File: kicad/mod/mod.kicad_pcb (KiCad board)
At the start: 2 copper layers, 9 parts, among them J1 In, J2 Out, J3 Program Pins, U1 AP7384-33SA, U2 ATtiny402-SS

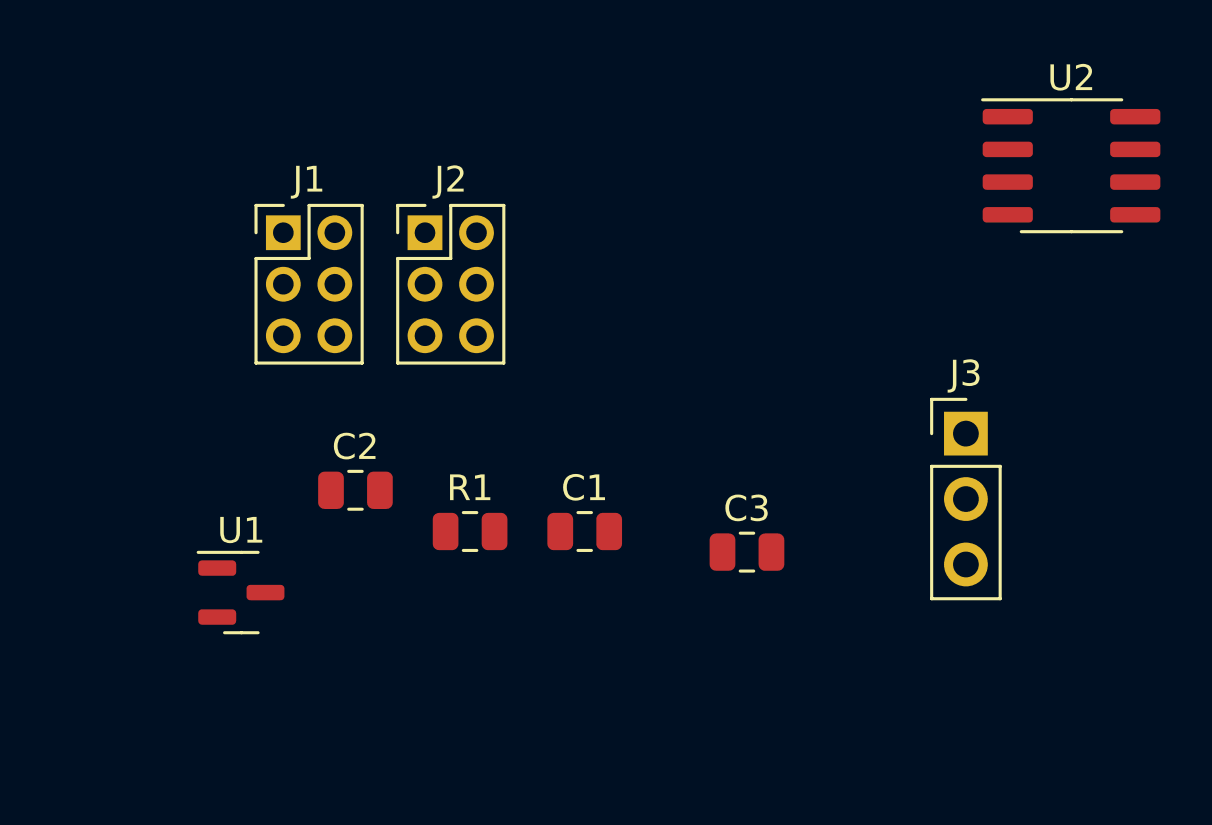
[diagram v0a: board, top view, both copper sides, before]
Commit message: Started layout
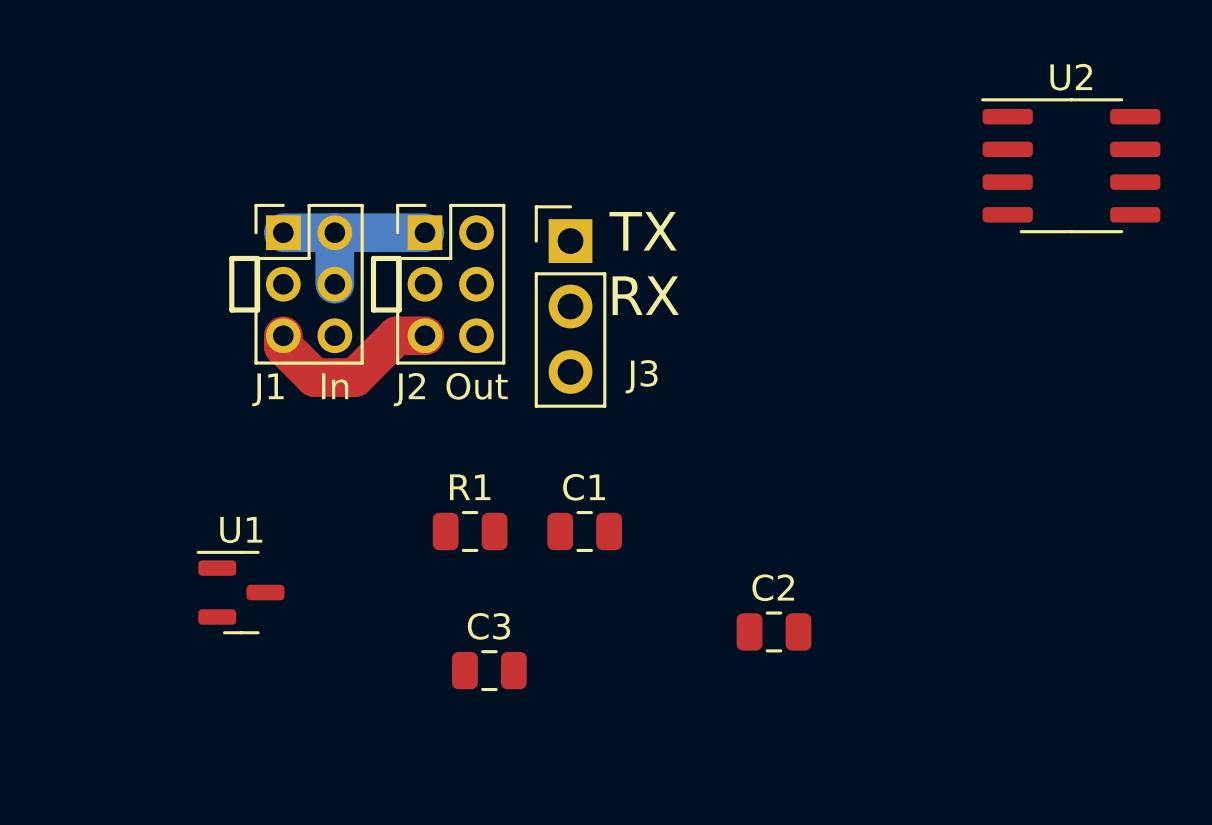
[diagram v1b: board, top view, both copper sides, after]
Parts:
- moved C2 17.2 mm to (147.1, 105.5)
- moved J3 17.1 mm to (139.2, 90.3)
- moved C3 11.0 mm to (136.0, 107.0)
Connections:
- J1 pad 1: +12V -> GND
- J1 pad 2: unconnected-(J1-Pad2) -> GND
- J1 pad 5: GND -> +12V
- J1 pad 6: GND -> unconnected-(J1-Pad6)
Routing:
- net GND: track 0.00 -> 7.50 mm
- net +12V: track 0.00 -> 7.08 mm
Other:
- board text added: "RX"
- board text added: "TX"
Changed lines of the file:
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@@
     (0 "F.Cu" signal)
     (31 "B.Cu" signal)
-    (32 "B.Adhes" user "B.Adhesive")
-    (33 "F.Adhes" user "F.Adhesive")
-    (34 "B.Paste" user)
-    (35 "F.Paste" user)
     (36 "B.SilkS" user "B.Silkscreen")
     (37 "F.SilkS" user "F.Silkscreen")
     (38 "B.Mask" user)
     (39 "F.Mask" user)
-    (40 "Dwgs.User" user "User.Drawings")
     (41 "Cmts.User" user "User.Comments")
     (42 "Eco1.User" user "User.Eco1")
@@
   )
   (setup
+    (stackup
+      (layer "F.SilkS" (type "Top Silk Screen"))
+      (layer "F.Mask" (type "Top Solder Mask") (color "Green") (thickness 0.01))
+      (layer "F.Cu" (type "copper") (thickness 0.035))
+      (layer "dielectric 1" (type "core") (thickness 1.51) (material "FR4") (epsilon_r 4.5) (loss_tangent 0.02))
+      (layer "B.Cu" (type "copper") (thickness 0.035))
+      (layer "B.Mask" (type "Bottom Solder Mask") (color "Green") (thickness 0.01))
+      (layer "B.SilkS" (type "Bottom Silk Screen"))
+      (copper_finish "None")
+      (dielectric_constraints no)
+    )
     (pcbplotparams
       (layerselection 0x00010fc_ffffffff)
@@
   (net 2 "Net-(C1-Pad1)")
   (net 3 "/PWM_IN")
-  (net 4 "unconnected-(J1-Pad2)")
+  (net 4 "unconnected-(J1-Pad6)")
   (net 5 "+12V")
   (net 6 "unconnected-(J2-Pad6)")
@@
   (net 14 "unconnected-(U2-Pad3)")
   (footprint "Connector_PinHeader_2.54mm:PinHeader_1x03_P2.54mm_Vertical" (layer "F.Cu")
-    (at 154.5 97.8)
+    (at 139.15 90.325)
     (descr "Through hole straight pin header, 1x03, 2.54mm pitch, single row")
     (tags "Through hole pin header THT 1x03 2.54mm single row")
@@
     (property "Sheetname" "")
     (attr through_hole)
-    (fp_text reference "J3" (at 0 -2.33) (layer "F.SilkS")
+    (fp_text reference "J3" (at 2.85 5.175) (layer "F.SilkS")
       (effects (font (size 1 1) (thickness 0.15)))
     )
@@
     (property "Sheetname" "")
     (attr through_hole)
-    (fp_text reference "J2" (at 1 -2.06) (layer "F.SilkS")
-      (effects (font (size 1 1) (thickness 0.15)))
-    )
-    (fp_text value "Out" (at 1 6.06) (layer "F.Fab")
+    (fp_text reference "J2" (at -0.5 6) (layer "F.SilkS")
+      (effects (font (size 1 1) (thickness 0.15)))
+    )
+    (fp_text value "Out" (at 2 6) (layer "F.SilkS")
       (effects (font (size 1 1) (thickness 0.15)))
     )
@@
     (property "Sheetname" "")
     (attr through_hole)
-    (fp_text reference "J1" (at 1 -2.06) (layer "F.SilkS")
-      (effects (font (size 1 1) (thickness 0.15)))
-    )
-    (fp_text value "In" (at 1 6.06) (layer "F.Fab")
+    (fp_text reference "J1" (at -0.5 6) (layer "F.SilkS")
+      (effects (font (size 1 1) (thickness 0.15)))
+    )
+    (fp_text value "In" (at 2 6) (layer "F.SilkS")
       (effects (font (size 1 1) (thickness 0.15)))
     )
@@
     (fp_line (start -1 0) (end 0 -1) (layer "F.Fab") (width 0.1))
     (pad "1" thru_hole rect (at 0 0) (locked) (size 1.35 1.35) (drill 0.8) (layers *.Cu *.Mask)
-      (net 5 "+12V") (pinfunction "Pin_1") (pintype "passive"))
+      (net 1 "GND") (pinfunction "Pin_1"))
     (pad "2" thru_hole oval (at 2 0) (locked) (size 1.35 1.35) (drill 0.8) (layers *.Cu *.Mask)
-      (net 4 "unconnected-(J1-Pad2)") (pinfunction "Pin_2") (pintype "passive+no_connect"))
+      (net 1 "GND") (pinfunction "Pin_2"))
     (pad "3" thru_hole oval (at 0 2) (locked) (size 1.35 1.35) (drill 0.8) (layers *.Cu *.Mask)
-      (net 3 "/PWM_IN") (pinfunction "Pin_3") (pintype "passive"))
+      (net 3 "/PWM_IN") (pinfunction "Pin_3"))
     (pad "4" thru_hole oval (at 2 2) (locked) (size 1.35 1.35) (drill 0.8) (layers *.Cu *.Mask)
-      (net 1 "GND") (pinfunction "Pin_4") (pintype "passive"))
+      (net 1 "GND") (pinfunction "Pin_4"))
     (pad "5" thru_hole oval (at 0 4) (locked) (size 1.35 1.35) (drill 0.8) (layers *.Cu *.Mask)
-      (net 1 "GND") (pinfunction "Pin_5") (pintype "passive"))
+      (net 5 "+12V") (pinfunction "Pin_5"))
     (pad "6" thru_hole oval (at 2 4) (locked) (size 1.35 1.35) (drill 0.8) (layers *.Cu *.Mask)
-      (net 1 "GND") (pinfunction "Pin_6") (pintype "passive"))
+      (net 4 "unconnected-(J1-Pad6)") (pinfunction "Pin_6"))
     (model "${KICAD6_3DMODEL_DIR}/Connector_PinHeader_2.00mm.3dshapes/PinHeader_2x03_P2.00mm_Vertical.wrl"
       (offset (xyz 0 0 0))
@@
   )
   (footprint "Capacitor_SMD:C_0805_2012Metric" (layer "F.Cu")
-    (at 130.8 100)
+    (at 147.05 105.5)
     (descr "Capacitor SMD 0805 (2012 Metric), square (rectangular) end terminal, IPC_7351 nominal, (Body size source: IPC-SM-782 page 76, https://www.pcb-3d.com/wordpress/wp-content/uploads/ipc-sm-782a_amendment_1_and_2.pdf, https://docs.google.com/spreadsheets/d/1BsfQQcO9C6DZCsRaXUlFlo91Tg2WpOkGARC1WS5S8t0/edit?usp=sharing), generated with kicad-footprint-generator")
     (tags "capacitor")
@@
   )
   (footprint "Capacitor_SMD:C_0805_2012Metric" (layer "F.Cu")
-    (at 146 102.4)
+    (at 136 107)
     (descr "Capacitor SMD 0805 (2012 Metric), square (rectangular) end terminal, IPC_7351 nominal, (Body size source: IPC-SM-782 page 76, https://www.pcb-3d.com/wordpress/wp-content/uploads/ipc-sm-782a_amendment_1_and_2.pdf, https://docs.google.com/spreadsheets/d/1BsfQQcO9C6DZCsRaXUlFlo91Tg2WpOkGARC1WS5S8t0/edit?usp=sharing), generated with kicad-footprint-generator")
     (tags "capacitor")
@@
     )
   )
+  (gr_rect (start 132.5 91) (end 131.5 93) (layer "F.SilkS") (width 0.2) (fill none))
+  (gr_rect (start 127 91) (end 126 93) (layer "F.SilkS") (width 0.2) (fill none))
+  (gr_text "RX" (at 142 92.5) (layer "F.SilkS")
+    (effects (font (size 1.5 1.5) (thickness 0.3)))
+  )
+  (gr_text "TX" (at 142 90) (layer "F.SilkS")
+    (effects (font (size 1.5 1.5) (thickness 0.3)))
+  )
+  (segment (start 130 92) (end 130 90) (width 1.5) (layer "B.Cu") (net 1))
+  (segment (start 130 90) (end 133.5 90) (width 1.5) (layer "B.Cu") (net 1))
+  (segment (start 128 90) (end 130 90) (width 1.5) (layer "B.Cu") (net 1))
+  (segment (start 129.219994 95.625011) (end 130.774989 95.625011) (width 1.5) (layer "F.Cu") (net 5))
+  (segment (start 128 94.405017) (end 129.219994 95.625011) (width 1.5) (layer "F.Cu") (net 5))
+  (segment (start 128 94) (end 128 94.405017) (width 1.5) (layer "F.Cu") (net 5))
+  (segment (start 132.4 94) (end 133.5 94) (width 1.5) (layer "F.Cu") (net 5))
+  (segment (start 130.774989 95.625011) (end 132.4 94) (width 1.5) (layer "F.Cu") (net 5))
 )

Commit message: Meh 2
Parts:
- added J4: I2C, Connector_PinHeader_2.54mm:PinHeader_1x03_P2.54mm_Vertical, F.Cu at (132.2, 98.0)
- added J5: I2C, Connector_PinHeader_2.54mm:PinHeader_1x03_P2.54mm_Vertical, F.Cu at (135.2, 98.0)
- C1, C3, R1, U1: moved to B.Cu
- moved U2 35.0 mm to (126.0, 100.0), turned to 90 degrees
- moved C2 25.9 mm to (121.8, 100.0), turned to -90 degrees
- moved J1 18.6 mm to (123.2, 108.0), turned to 90 degrees
- moved C1 15.7 mm to (124.0, 102.8), turned to -90 degrees
- moved C3 14.8 mm to (125.5, 96.6), turned to 180 degrees
- moved J2 11.1 mm to (123.2, 94.2), turned to 90 degrees
- moved R1 8.85 mm to (140.4, 94.4), turned to -90 degrees
- moved U1 4.52 mm to (125.2, 99.6), turned to 180 degrees
- moved J3 2.82 mm to (138.2, 93.0)
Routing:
- net GND: track 7.50 -> 43.3 mm, vias 0 -> 1
- net +12V: track 7.08 -> 21.7 mm
- net /SDA: track 0.00 -> 10.4 mm
- net Net-(C1-Pad1): track 0.00 -> 10.2 mm, vias 0 -> 1
- net /SCL: track 0.00 -> 9.11 mm
- net Net-(J3-Pad1): track 0.00 -> 2.40 mm
- net Net-(J3-Pad2): track 0.00 -> 2.27 mm
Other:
- board outline added: 21.5 x 20 mm
- board text added: "GND"
- board text added: "IN"
- board text added: "OUT"
- board text added: "SCL"
- board text added: "SDA"

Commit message: Yeeet
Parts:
- moved C1 0.94 mm to (124.8, 103.2), turned to 180 degrees
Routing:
- net GND: track 43.3 -> 0.00 mm, vias 1 -> 4
- net /PWM_IN: track 0.00 -> 6.29 mm
- net /PWM_OUT: track 0.00 -> 3.36 mm
- net Net-(C1-Pad1): track 10.2 -> 12.2 mm
- added copper zone on B.Cu, net GND
- added copper zone on F.Cu, net GND

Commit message: Kinda complete
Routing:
- net Net-(J3-Pad2): track 2.27 -> 16.4 mm
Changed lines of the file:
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@@
   (via (at 121.8 96.8) (size 0.8) (drill 0.5) (layers "F.Cu" "B.Cu") (free) (net 1))
   (via (at 122.4 103.8) (size 0.8) (drill 0.5) (layers "F.Cu" "B.Cu") (free) (net 1))
-  (via (at 129.6 93.6) (size 0.8) (drill 0.5) (layers "F.Cu" "B.Cu") (free) (net 1))
+  (via (at 129.571258 93.484979) (size 0.8) (drill 0.5) (layers "F.Cu" "B.Cu") (free) (net 1))
   (segment (start 121.75 101.75) (end 122.475 102.475) (width 0.25) (layer "F.Cu") (net 2))
   (segment (start 122.475 102.475) (end 124.095 102.475) (width 0.25) (layer "F.Cu") (net 2))
@@
   (segment (start 125.365 95.765) (end 125.2 95.6) (width 0.35) (layer "F.Cu") (net 8))
   (segment (start 125.2 94.3) (end 125.25 94.25) (width 0.35) (layer "F.Cu") (net 8))
+  (segment (start 129.540011 94.259989) (end 128.1 95.7) (width 0.35) (layer "F.Cu") (net 10))
+  (segment (start 126.635 96.365) (end 126.635 97.525) (width 0.35) (layer "F.Cu") (net 10))
+  (segment (start 138.2 95.515) (end 137.215 95.515) (width 0.35) (layer "F.Cu") (net 10))
+  (segment (start 137.215 95.515) (end 135.959989 94.259989) (width 0.35) (layer "F.Cu") (net 10))
+  (segment (start 127.3 95.7) (end 126.635 96.365) (width 0.35) (layer "F.Cu") (net 10))
+  (segment (start 135.959989 94.259989) (end 129.540011 94.259989) (width 0.35) (layer "F.Cu") (net 10))
+  (segment (start 128.1 95.7) (end 127.3 95.7) (width 0.35) (layer "F.Cu") (net 10))
   (segment (start 138.365 95.35) (end 138.2 95.515) (width 0.35) (layer "B.Cu") (net 10))
   (segment (start 140.4 95.35) (end 138.365 95.35) (width 0.35) (layer "B.Cu") (net 10))
@@
   (segment (start 140.4 93.45) (end 139.65 93.45) (width 0.35) (layer "B.Cu") (net 11))
   (segment (start 139.65 93.45) (end 139.175 92.975) (width 0.35) (layer "B.Cu") (net 11))
-  (segment (start 127.905 97.525) (end 127.905 95.895) (width 0.35) (layer "F.Cu") (net 12))
-  (segment (start 127.905 95.895) (end 128.315 95.485) (width 0.35) (layer "F.Cu") (net 12))
-  (segment (start 128.315 95.485) (end 132.2 95.485) (width 0.35) (layer "F.Cu") (net 12))
+  (segment (start 131.985 95.7) (end 132.2 95.485) (width 0.35) (layer "F.Cu") (net 12))
+  (segment (start 128.9 95.7) (end 131.985 95.7) (width 0.35) (layer "F.Cu") (net 12))
+  (segment (start 127.905 96.695) (end 128.9 95.7) (width 0.35) (layer "F.Cu") (net 12))
+  (segment (start 127.905 97.525) (end 127.905 96.695) (width 0.35) (layer "F.Cu") (net 12))
   (segment (start 135.2 95.51) (end 132.225 95.51) (width 0.35) (layer "B.Cu") (net 12))
   (segment (start 132.225 95.51) (end 132.2 95.485) (width 0.35) (layer "B.Cu") (net 12))
